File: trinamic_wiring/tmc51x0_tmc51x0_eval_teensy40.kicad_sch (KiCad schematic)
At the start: 4 parts, among them M1 Stepper_Motor

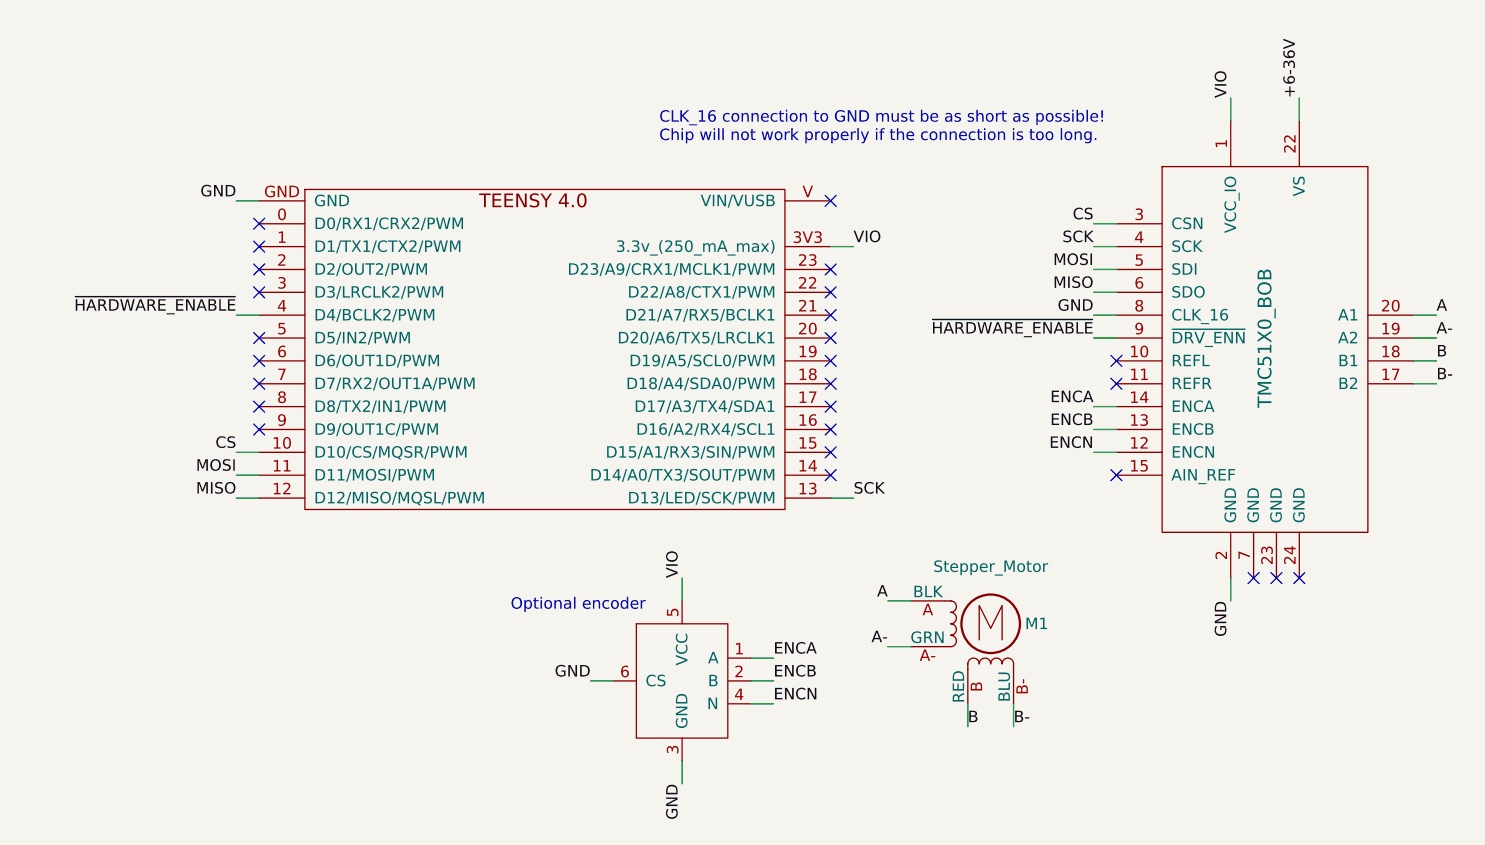
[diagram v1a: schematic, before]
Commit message: miso -> cipo, mosi -> copi
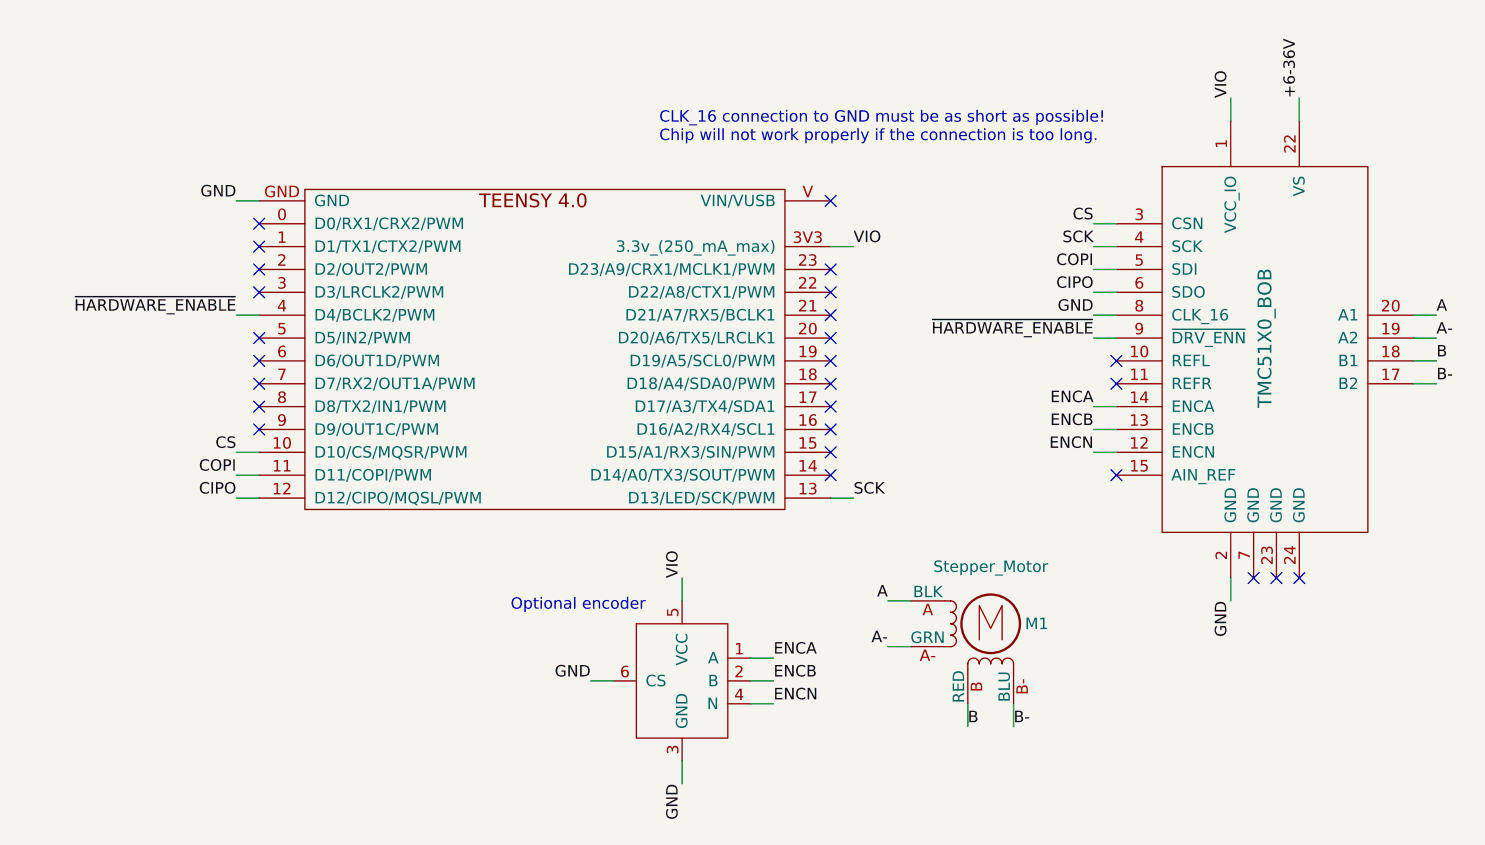
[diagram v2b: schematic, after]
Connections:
- net MISO renamed CIPO
- net MOSI renamed COPI
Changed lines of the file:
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@@
     (effects (font (size 1.27 1.27)) (justify right bottom))
   )
-  (label "MISO" (at 161.29 96.52 180) (fields_autoplaced)
+  (label "CIPO" (at 161.29 96.52 180) (fields_autoplaced)
     (effects (font (size 1.27 1.27)) (justify right bottom))
   )
@@
     (effects (font (size 1.27 1.27)) (justify right bottom))
   )
-  (label "MOSI" (at 161.29 93.98 180) (fields_autoplaced)
+  (label "COPI" (at 161.29 93.98 180) (fields_autoplaced)
     (effects (font (size 1.27 1.27)) (justify right bottom))
   )
@@
     (effects (font (size 1.27 1.27)) (justify left bottom))
   )
-  (label "MOSI" (at 66.04 116.84 180) (fields_autoplaced)
+  (label "COPI" (at 66.04 116.84 180) (fields_autoplaced)
     (effects (font (size 1.27 1.27)) (justify right bottom))
   )
-  (label "MISO" (at 66.04 119.38 180) (fields_autoplaced)
+  (label "CIPO" (at 66.04 119.38 180) (fields_autoplaced)
     (effects (font (size 1.27 1.27)) (justify right bottom))
   )
